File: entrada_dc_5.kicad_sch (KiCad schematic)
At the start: 4 parts

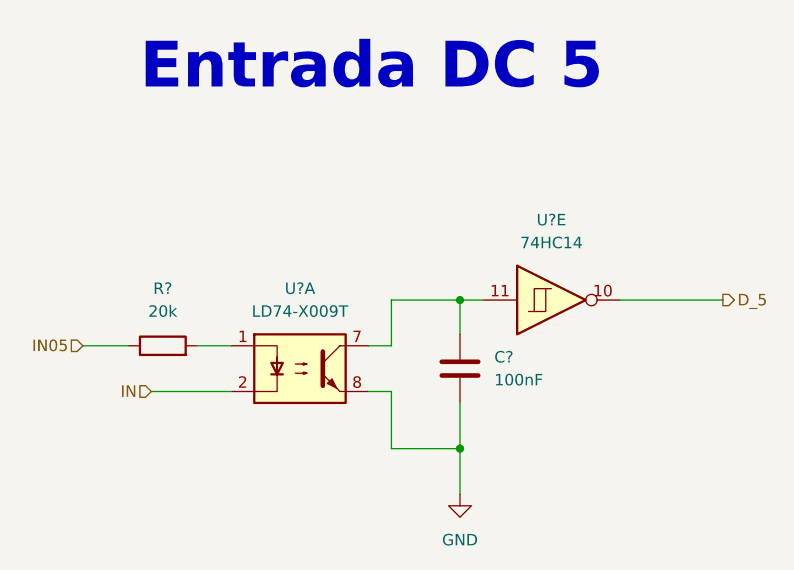
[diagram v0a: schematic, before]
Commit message: input/output separadas
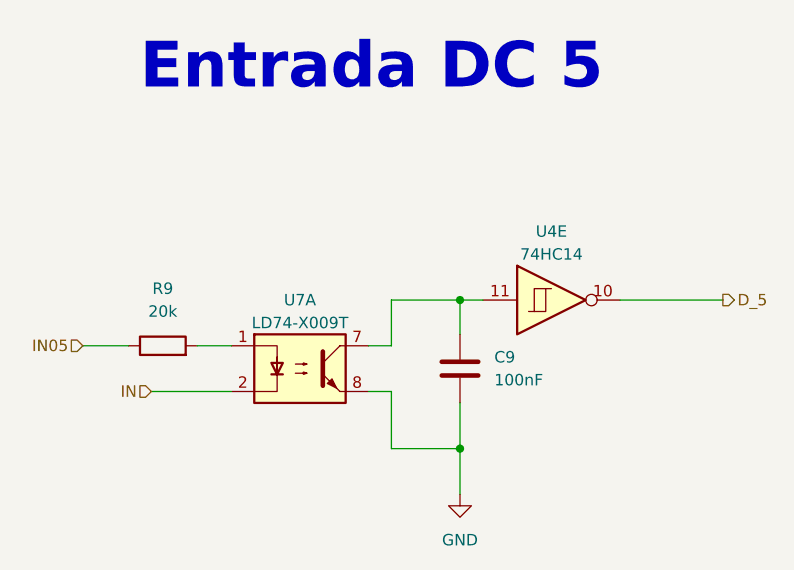
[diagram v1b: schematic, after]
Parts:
- gave numbers to parts that had none: 4
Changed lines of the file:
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@@
 (kicad_sch (version 20221004) (generator eeschema)
   (paper "A4" portrait)
+  (title_block
+    (date "2022-10-09")
+    (rev "José Luis Laica")
+  )
   (junction (at 110.49 140.97) (diameter 0) (color 0 0 0 0)
   )
@@
   (symbol (lib_id "Isolator:ILD74") (at 92.71 148.59 0) (unit 1)
     (in_bom yes) (on_board yes) (dnp no) (fields_autoplaced)
-    (property "Reference" "U?" (at 92.71 139.7 0)
+    (property "Reference" "U7" (at 92.71 140.97 0)
       (effects (font (size 1.27 1.27)))
     )
-    (property "Value" "LD74-X009T" (at 92.71 142.24 0)
+    (property "Value" "LD74-X009T" (at 92.71 143.51 0)
       (effects (font (size 1.27 1.27)))
     )
@@
       (project "PLC 32 V2"
         (path "/d17a54f1-6eda-453f-95e1-42a53b02a1c3/a6d2e040-0a94-4a2e-860d-bf58d3405101"
-          (reference "U?") (unit 1) (value "LD74-X009T") (footprint "Package_DIP:DIP-8_W8.89mm_SMDSocket_LongPads")
+          (reference "U7") (unit 1) (value "LD74-X009T") (footprint "Package_DIP:DIP-8_W8.89mm_SMDSocket_LongPads")
         )
       )
@@
   (symbol (lib_id "power:GND") (at 110.49 162.56 0) (unit 1)
     (in_bom yes) (on_board yes) (dnp no) (fields_autoplaced)
-    (property "Reference" "#PWR?" (at 110.49 168.91 0)
+    (property "Reference" "#PWR010" (at 110.49 168.91 0)
       (effects (font (size 1.27 1.27)) hide)
     )
@@
       (project "PLC 32 V2"
         (path "/d17a54f1-6eda-453f-95e1-42a53b02a1c3/a6d2e040-0a94-4a2e-860d-bf58d3405101"
-          (reference "#PWR?") (unit 1) (value "GND") (footprint "")
+          (reference "#PWR010") (unit 1) (value "GND") (footprint "")
         )
       )
@@
   (symbol (lib_id "74xx:74HC14") (at 120.65 140.97 0) (unit 5)
     (in_bom yes) (on_board yes) (dnp no) (fields_autoplaced)
-    (property "Reference" "U?" (at 120.65 132.08 0)
+    (property "Reference" "U4" (at 120.65 133.35 0)
       (effects (font (size 1.27 1.27)))
     )
-    (property "Value" "74HC14" (at 120.65 134.62 0)
+    (property "Value" "74HC14" (at 120.65 135.89 0)
       (effects (font (size 1.27 1.27)))
     )
@@
       (project "PLC 32 V2"
         (path "/d17a54f1-6eda-453f-95e1-42a53b02a1c3/a6d2e040-0a94-4a2e-860d-bf58d3405101"
-          (reference "U?") (unit 5) (value "74HC14") (footprint "Package_SO:SOIC-14W_7.5x9mm_P1.27mm")
+          (reference "U4") (unit 5) (value "74HC14") (footprint "Package_SO:SOIC-14W_7.5x9mm_P1.27mm")
         )
       )
@@
   (symbol (lib_id "Device:C") (at 110.49 148.59 0) (unit 1)
     (in_bom yes) (on_board yes) (dnp no) (fields_autoplaced)
-    (property "Reference" "C?" (at 114.3 147.3199 0)
+    (property "Reference" "C9" (at 114.3 147.3199 0)
       (effects (font (size 1.27 1.27)) (justify left))
     )
@@
       (project "PLC 32 V2"
         (path "/d17a54f1-6eda-453f-95e1-42a53b02a1c3/a6d2e040-0a94-4a2e-860d-bf58d3405101"
-          (reference "C?") (unit 1) (value "100nF") (footprint "Capacitor_SMD:C_0402_1005Metric")
+          (reference "C9") (unit 1) (value "100nF") (footprint "Capacitor_SMD:C_0402_1005Metric")
         )
       )
@@
   (symbol (lib_id "Device:R") (at 77.47 146.05 90) (unit 1)
     (in_bom yes) (on_board yes) (dnp no) (fields_autoplaced)
-    (property "Reference" "R?" (at 77.47 139.7 90)
+    (property "Reference" "R9" (at 77.47 139.7 90)
       (effects (font (size 1.27 1.27)))
     )
@@
       (project "PLC 32 V2"
         (path "/d17a54f1-6eda-453f-95e1-42a53b02a1c3/a6d2e040-0a94-4a2e-860d-bf58d3405101"
-          (reference "R?") (unit 1) (value "20k") (footprint "Resistor_SMD:R_0603_1608Metric")
+          (reference "R9") (unit 1) (value "20k") (footprint "Resistor_SMD:R_0603_1608Metric")
         )
       )

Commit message: add
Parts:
- renumbered C9 to C10, R9 to R39, U7 to U10, U4 to U7
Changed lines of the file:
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@@
   (symbol (lib_id "Isolator:ILD74") (at 92.71 148.59 0) (unit 1)
     (in_bom yes) (on_board yes) (dnp no) (fields_autoplaced)
-    (property "Reference" "U7" (at 92.71 140.97 0)
+    (property "Reference" "U10" (at 92.71 140.97 0)
       (effects (font (size 1.27 1.27)))
     )
@@
       (project "PLC 32 V2"
         (path "/d17a54f1-6eda-453f-95e1-42a53b02a1c3/a6d2e040-0a94-4a2e-860d-bf58d3405101"
-          (reference "U7") (unit 1) (value "LD74-X009T") (footprint "Package_DIP:DIP-8_W8.89mm_SMDSocket_LongPads")
+          (reference "U10") (unit 1) (value "LD74-X009T") (footprint "Package_DIP:DIP-8_W8.89mm_SMDSocket_LongPads")
         )
       )
@@
   (symbol (lib_id "74xx:74HC14") (at 120.65 140.97 0) (unit 5)
     (in_bom yes) (on_board yes) (dnp no) (fields_autoplaced)
-    (property "Reference" "U4" (at 120.65 133.35 0)
+    (property "Reference" "U7" (at 120.65 133.35 0)
       (effects (font (size 1.27 1.27)))
     )
@@
       (project "PLC 32 V2"
         (path "/d17a54f1-6eda-453f-95e1-42a53b02a1c3/a6d2e040-0a94-4a2e-860d-bf58d3405101"
-          (reference "U4") (unit 5) (value "74HC14") (footprint "Package_SO:SOIC-14W_7.5x9mm_P1.27mm")
+          (reference "U7") (unit 5) (value "74HC14") (footprint "Package_SO:SOIC-14W_7.5x9mm_P1.27mm")
         )
       )
@@
   (symbol (lib_id "Device:C") (at 110.49 148.59 0) (unit 1)
     (in_bom yes) (on_board yes) (dnp no) (fields_autoplaced)
-    (property "Reference" "C9" (at 114.3 147.3199 0)
+    (property "Reference" "C10" (at 114.3 147.3199 0)
       (effects (font (size 1.27 1.27)) (justify left))
     )
@@
       (project "PLC 32 V2"
         (path "/d17a54f1-6eda-453f-95e1-42a53b02a1c3/a6d2e040-0a94-4a2e-860d-bf58d3405101"
-          (reference "C9") (unit 1) (value "100nF") (footprint "Capacitor_SMD:C_0402_1005Metric")
+          (reference "C10") (unit 1) (value "100nF") (footprint "Capacitor_SMD:C_0402_1005Metric")
         )
       )
@@
   (symbol (lib_id "Device:R") (at 77.47 146.05 90) (unit 1)
     (in_bom yes) (on_board yes) (dnp no) (fields_autoplaced)
-    (property "Reference" "R9" (at 77.47 139.7 90)
+    (property "Reference" "R39" (at 77.47 139.7 90)
       (effects (font (size 1.27 1.27)))
     )
@@
       (project "PLC 32 V2"
         (path "/d17a54f1-6eda-453f-95e1-42a53b02a1c3/a6d2e040-0a94-4a2e-860d-bf58d3405101"
-          (reference "R9") (unit 1) (value "20k") (footprint "Resistor_SMD:R_0603_1608Metric")
+          (reference "R39") (unit 1) (value "20k") (footprint "Resistor_SMD:R_0603_1608Metric")
         )
       )
